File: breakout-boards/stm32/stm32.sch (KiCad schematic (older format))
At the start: 24 parts, among them J1 Conn_ARM_JTAG_SWD_10, J2 AudioJack4, J3 CONN_LEFT, J4 CONN_RIGHT, J5 USB_SENSE, P1 USB_C, SW1 RST_SW, U1 AP2127N-3.3, U2 STM32F042K6Tx, Y1 16MHz

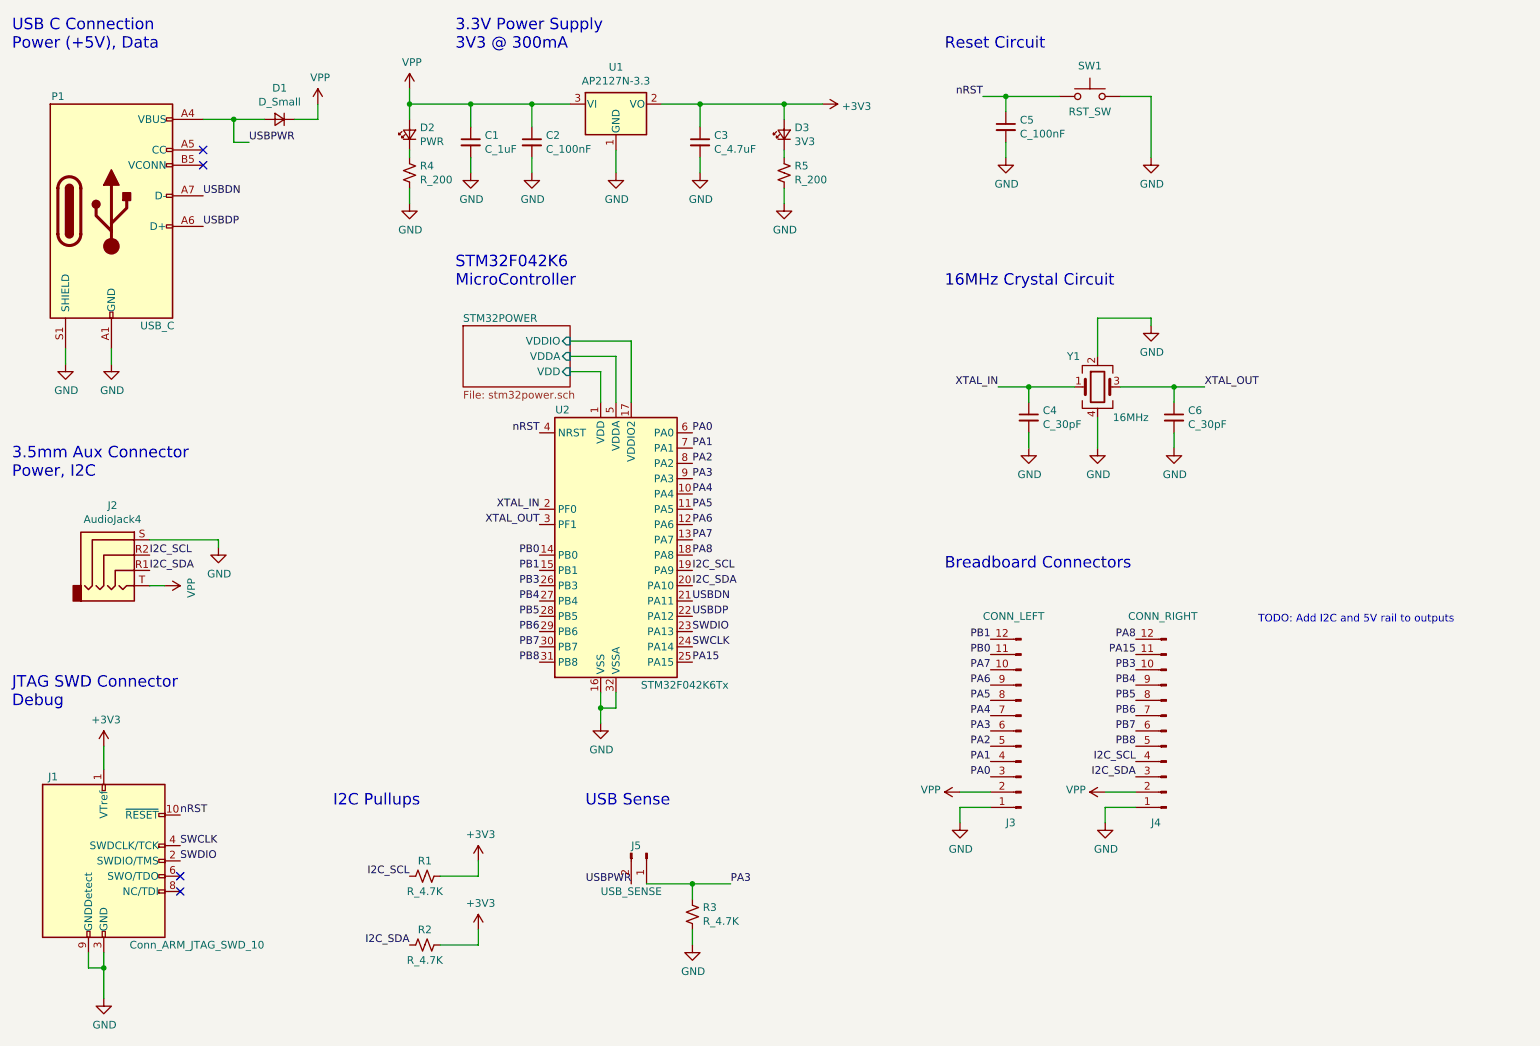
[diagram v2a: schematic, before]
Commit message: (#14) redo stm32 and eeprom board to only include 0603 and 0805 components
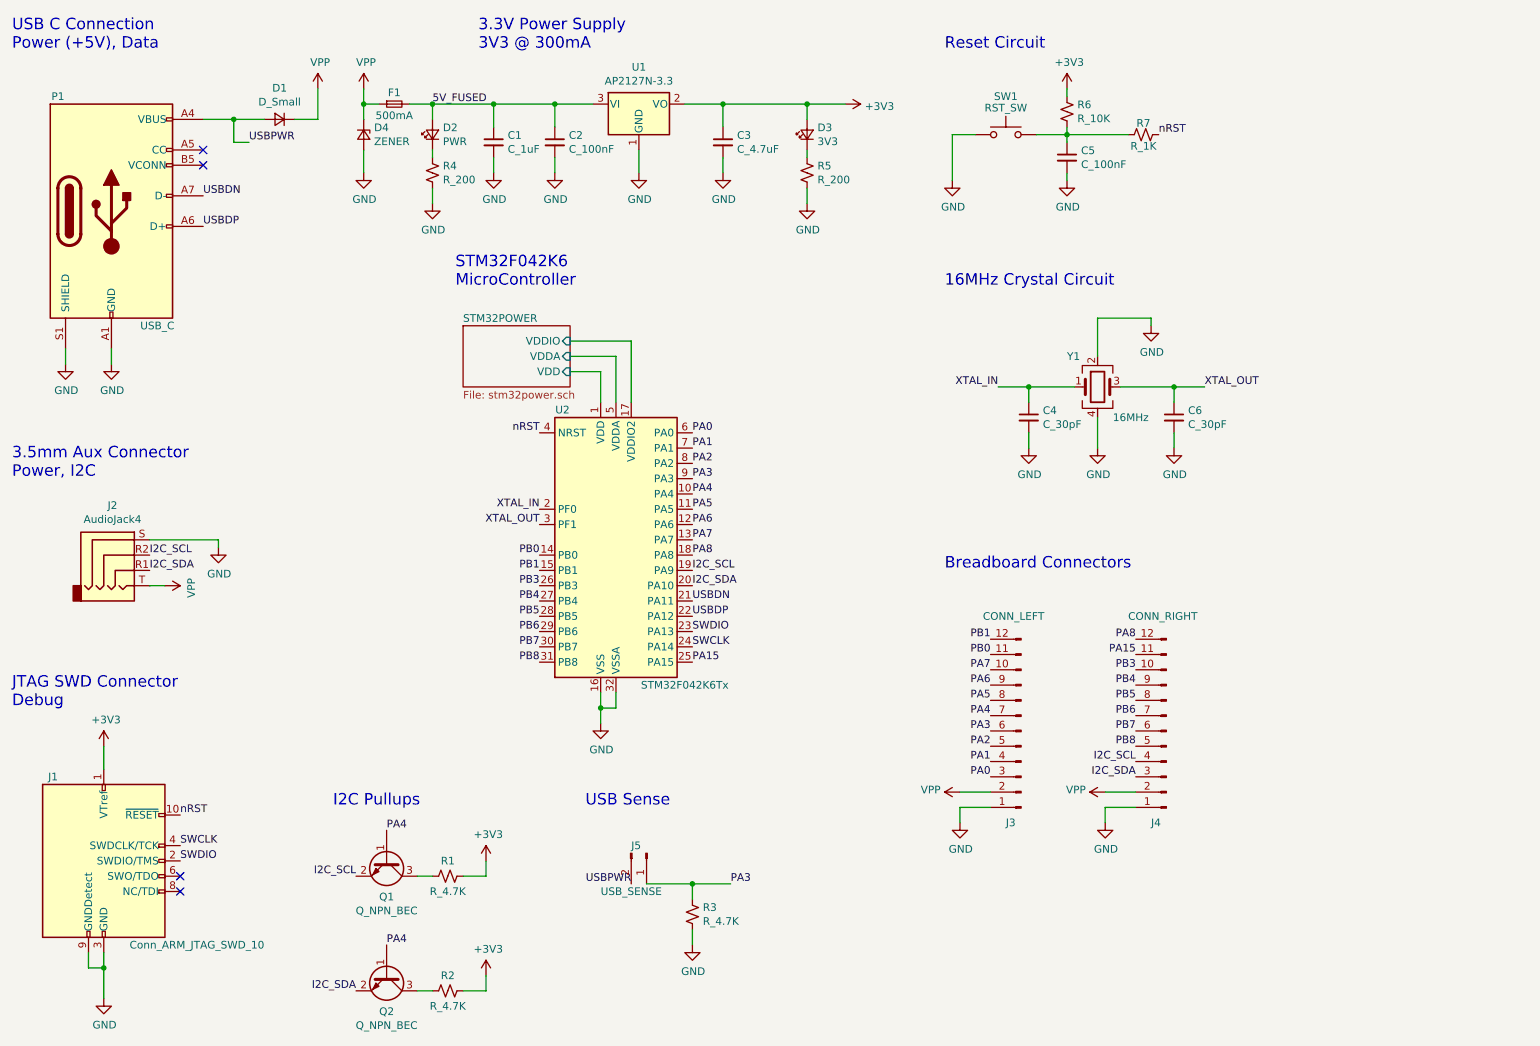
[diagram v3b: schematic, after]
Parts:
- added D4: ZENER, ultraboard:DO-214AA, symbol Device:D_Zener_Small
- added F1: 500mA, Fuse:Fuse_1206_3216Metric, symbol Device:Fuse_Small
- added Q1, Q2: Q_NPN_BEC, Package_TO_SOT_SMD:SOT-23, symbol Device:Q_NPN_BEC
- added R6: R_10K, Resistor_SMD:R_0603_1608Metric, symbol ultraboard_lib:R_10K
- added R7: R_1K, Resistor_SMD:R_0603_1608Metric, symbol ultraboard_lib:R_1K
- C1, C3: footprint Capacitor_SMD:C_0402_1005Metric -> Capacitor_SMD:C_0603_1608Metric
- C2, C4, C5, C6: footprint Capacitor_SMD:C_0201_0603Metric -> Capacitor_SMD:C_0603_1608Metric
- R1, R2, R3, R4, R5: footprint Resistor_SMD:R_0402_1005Metric -> Resistor_SMD:R_0603_1608Metric
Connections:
- net +3V3: now also R6.1
- net GND: now also SW1.1, D4.2 (A); no longer SW1.2
- net I2C_SCL: now also Q1.2 (E); no longer R1.2
- net I2C_SDA: now also Q2.2 (E); no longer R2.2
- net PA4: now also Q1.1 (B), Q2.1 (B)
- net VPP: now also D4.1 (K), F1.1; no longer C1.1, C2.1, D2.2 (A), U1.3 (VI)
- net nRST: now also R7.1; no longer C5.1, SW1.1
- new net: C5.1, R6.2, R7.2, SW1.2
- new net: Q1.3 (C), R1.2
- new net: Q2.3 (C), R2.2
- new net 5V_FUSED: C1.1, C2.1, D2.2 (A), F1.2, U1.3 (VI)
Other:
- note removed: "TODO: Add I2C and 5V rail to outputs"
- moved on the sheet: C1, C2, C3, C5, D2, D3, R1, R2, R4, R5, SW1, U1

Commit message: switch jtag header from smd to pth
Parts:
- J1: footprint Connector_PinHeader_1.27mm:PinHeader_2x05_P1.27mm_Vertical_SMD -> Connector_PinHeader_1.27mm:PinHeader_2x05_P1.27mm_Vertical
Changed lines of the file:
@@
 F 0 "J1" H 1200 6900 50  0000 R CNN
 F 1 "Conn_ARM_JTAG_SWD_10" H 2550 5800 50  0000 R CNN
-F 2 "Connector_PinHeader_1.27mm:PinHeader_2x05_P1.27mm_Vertical_SMD" H 1500 6350 50  0001 C CNN
+F 2 "Connector_PinHeader_1.27mm:PinHeader_2x05_P1.27mm_Vertical" H 1500 6350 50  0001 C CNN
 F 3 "http://infocenter.arm.com/help/topic/com.arm.doc.ddi0314h/DDI0314H_coresight_components_trm.pdf" V 1150 5100 50  0001 C CNN
 	1    1500 6350
